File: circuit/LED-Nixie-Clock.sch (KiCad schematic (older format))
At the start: 16 parts, among them SW1 Reset, U1 LM1117-3.3, U2 STM32F103C8Tx

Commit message: Improve schematics, add crystals, USB connector, power regulator, backup battery
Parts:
- added BT1: 3V, Battery:BatteryHolder_Keystone_1058_1x2032, symbol Device:Battery_Cell
- added C10, C11, C12, C13: 20p, Capacitor_SMD:C_0805_2012Metric_Pad1.15x1.40mm_HandSolder, symbol Device:C
- added C5: 100n, Capacitor_SMD:C_0805_2012Metric_Pad1.15x1.40mm_HandSolder, symbol Device:C
- added D1, D2: 1N5817, Diode_SMD:D_0805_2012Metric_Pad1.15x1.40mm_HandSolder, symbol Device:D_Schottky
- added J1: USB Micro, Connector_USB:USB_Micro-B_Molex_47346-0001, symbol Connector:USB_B_Micro
- added R2: 20R, Resistor_SMD:R_0805_2012Metric_Pad1.15x1.40mm_HandSolder, symbol Device:R
- added R3: 4.7k, Resistor_SMD:R_0805_2012Metric_Pad1.15x1.40mm_HandSolder, symbol Device:R
- added Y1: 8MHz, Crystal:Crystal_SMD_HC49-SD, symbol Device:Crystal
- added Y2: 32.768kHz, Crystal:Crystal_SMD_3225-4Pin_3.2x2.5mm, symbol Device:Crystal
- C1, C2, C3, C4: footprint Capacitor_SMD:C_0805_2012Metric -> Capacitor_SMD:C_0805_2012Metric_Pad1.15x1.40mm_HandSolder
- C14: renamed from C9; value 100n -> 1u; footprint Capacitor_SMD:C_0805_2012Metric -> Capacitor_SMD:C_0805_2012Metric_Pad1.15x1.40mm_HandSolder
- C6: renamed from C5; footprint Capacitor_SMD:C_0805_2012Metric -> Capacitor_SMD:C_0805_2012Metric_Pad1.15x1.40mm_HandSolder
- C7: renamed from C6; footprint Capacitor_SMD:C_0805_2012Metric -> Capacitor_SMD:C_0805_2012Metric_Pad1.15x1.40mm_HandSolder
- C8: renamed from C7; footprint Capacitor_SMD:C_0805_2012Metric -> Capacitor_SMD:C_0805_2012Metric_Pad1.15x1.40mm_HandSolder
- C9: renamed from C8; footprint Capacitor_SMD:C_0805_2012Metric -> Capacitor_SMD:C_0805_2012Metric_Pad1.15x1.40mm_HandSolder
- R1: value 10k -> 20R; footprint Resistor_SMD:R_0805_2012Metric -> Resistor_SMD:R_0805_2012Metric_Pad1.15x1.40mm_HandSolder
- R4: renamed from R2; footprint Resistor_SMD:R_0805_2012Metric -> Resistor_SMD:R_0805_2012Metric_Pad1.15x1.40mm_HandSolder
- R5: renamed from R3; footprint Resistor_SMD:R_0805_2012Metric -> Resistor_SMD:R_0805_2012Metric_Pad1.15x1.40mm_HandSolder
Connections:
- net labels added: +BATT, OSC32_IN, OSC32_OUT, OSC_IN, OSC_OUT, USBDM, USBDP, VBUS
- net labels removed: VCC, VDC
- wire segments 54 -> 103
- no-connect marks 37 -> 31
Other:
- moved on the sheet: C1, C14, C2, C3, C4, C6, C7, C8, C9, JP1, R4, R5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

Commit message: Add a test point at DOUT of the last LED
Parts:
- added TP1: DOUT, TestPoint:TestPoint_Pad_1.0x1.0mm, symbol Connector:TestPoint
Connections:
- no-connect marks 31 -> 30
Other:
- moved on the sheet: C6, C7, C8, C9, R5, U2

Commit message: Use MCP1700 linear regulator instead of LM1117
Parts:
- removed C2, C4: 100n, Capacitor_SMD:C_0805_2012Metric_Pad1.15x1.40mm_HandSolder, symbol Device:C
- removed U1: LM1117-3.3, Package_TO_SOT_SMD:SOT-223-3_TabPin2, symbol Regulator_Linear:LM1117-3.3
- added U1: MCP1700-3302E_SOT23, Package_TO_SOT_SMD:SOT-23_Handsoldering, symbol Regulator_Linear:MCP1700-3302E_SOT23
- C2: renamed from C3; value 10u -> 1u
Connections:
- wire segments 103 -> 95
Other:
- moved on the sheet: C2
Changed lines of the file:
@@
 L power:VDD #PWR0110
 U 1 1 5C3A07BC
-P 4800 900
-F 0 "#PWR0110" H 4800 750 50  0001 C CNN
-F 1 "VDD" H 4817 1073 50  0000 C CNN
-F 2 "" H 4800 900 50  0001 C CNN
-F 3 "" H 4800 900 50  0001 C CNN
-	1    4800 900
+P 4100 900
+F 0 "#PWR0110" H 4100 750 50  0001 C CNN
+F 1 "VDD" H 4117 1073 50  0000 C CNN
+F 2 "" H 4100 900 50  0001 C CNN
+F 3 "" H 4100 900 50  0001 C CNN
+	1    4100 900
 	1    0    0    -1
 $EndComp
@@
 	4900 5200 4800 5200
 $Comp
-L Regulator_Linear:LM1117-3.3 U1
-U 1 1 5C415EF9
-P 3900 900
-F 0 "U1" H 3900 1142 50  0000 C CNN
-F 1 "LM1117-3.3" H 3900 1051 50  0000 C CNN
-F 2 "Package_TO_SOT_SMD:SOT-223-3_TabPin2" H 3900 900 50  0001 C CNN
-F 3 "http://www.ti.com/lit/ds/symlink/lm1117.pdf" H 3900 900 50  0001 C CNN
-	1    3900 900
-	1    0    0    -1
-$EndComp
-$Comp
-L Device:C C3
+L Device:C C2
 U 1 1 5C424CF6
-P 4400 1250
-F 0 "C3" H 4515 1296 50  0000 L CNN
-F 1 "10u" H 4515 1205 50  0000 L CNN
-F 2 "Capacitor_SMD:C_0805_2012Metric_Pad1.15x1.40mm_HandSolder" H 4438 1100 50  0001 C CNN
-F 3 "~" H 4400 1250 50  0001 C CNN
-	1    4400 1250
-	1    0    0    -1
-$EndComp
-$Comp
-L Device:C C4
-U 1 1 5C424ED1
-P 4800 1250
-F 0 "C4" H 4915 1296 50  0000 L CNN
-F 1 "100n" H 4915 1205 50  0000 L CNN
-F 2 "Capacitor_SMD:C_0805_2012Metric_Pad1.15x1.40mm_HandSolder" H 4838 1100 50  0001 C CNN
-F 3 "~" H 4800 1250 50  0001 C CNN
-	1    4800 1250
-	1    0    0    -1
-$EndComp
-$Comp
-L Device:C C2
-U 1 1 5C4295B3
-P 3300 1250
-F 0 "C2" H 3415 1296 50  0000 L CNN
-F 1 "100n" H 3415 1205 50  0000 L CNN
-F 2 "Capacitor_SMD:C_0805_2012Metric_Pad1.15x1.40mm_HandSolder" H 3338 1100 50  0001 C CNN
-F 3 "~" H 3300 1250 50  0001 C CNN
-	1    3300 1250
+P 4100 1250
+F 0 "C2" H 4215 1296 50  0000 L CNN
+F 1 "1u" H 4215 1205 50  0000 L CNN
+F 2 "Capacitor_SMD:C_0805_2012Metric_Pad1.15x1.40mm_HandSolder" H 4138 1100 50  0001 C CNN
+F 3 "~" H 4100 1250 50  0001 C CNN
+	1    4100 1250
 	1    0    0    -1
 $EndComp
@@
 	2900 900  2900 1100
 Wire Wire Line
-	4200 900  4400 900
-Wire Wire Line
-	2900 900  3300 900
+	3800 900  4100 900
+Wire Wire Line
+	2900 900  3200 900
 Wire Wire Line
 	2900 1400 2900 1600
 Wire Wire Line
-	2900 1600 3300 1600
-Wire Wire Line
-	3300 1100 3300 900
-Connection ~ 3300 900
-Wire Wire Line
-	3300 900  3600 900
-Wire Wire Line
-	3300 1400 3300 1600
-Connection ~ 3300 1600
-Wire Wire Line
-	3300 1600 3900 1600
-Wire Wire Line
-	4400 1100 4400 900
-Connection ~ 4400 900
-Wire Wire Line
-	4400 900  4800 900
-Wire Wire Line
-	3900 1200 3900 1600
-Connection ~ 3900 1600
-Wire Wire Line
-	3900 1600 4400 1600
-Wire Wire Line
-	4400 1400 4400 1600
-Connection ~ 4400 1600
-Wire Wire Line
-	4400 1600 4800 1600
-Wire Wire Line
-	4800 1400 4800 1600
-Wire Wire Line
-	4800 1100 4800 900
-Connection ~ 4800 900
-Connection ~ 2900 1600
+	4100 1100 4100 900
+Connection ~ 4100 900
+Wire Wire Line
+	3500 1200 3500 1600
+Wire Wire Line
+	3500 1600 4100 1600
+Wire Wire Line
+	4100 1400 4100 1600
 Wire Wire Line
 	2500 900  2900 900
@@
 	0    1    1    0
 $EndComp
+$Comp
+L Regulator_Linear:MCP1700-3302E_SOT23 U1
+U 1 1 5C8BC8BE
+P 3500 900
+F 0 "U1" H 3500 1142 50  0000 C CNN
+F 1 "MCP1700-3302E_SOT23" H 3500 1051 50  0000 C CNN
+F 2 "Package_TO_SOT_SMD:SOT-23_Handsoldering" H 3500 1125 50  0001 C CNN
+F 3 "http://ww1.microchip.com/downloads/en/DeviceDoc/20001826C.pdf" H 3500 900 50  0001 C CNN
+	1    3500 900
+	1    0    0    -1
+$EndComp
+Wire Wire Line
+	2900 1600 3500 1600
+Connection ~ 2900 1600
+Connection ~ 3500 1600
 $EndSCHEMATC

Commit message: Add mounting holes
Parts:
- added H1, H2, H3, H4, H5, H6: MountingHole, MountingHole:MountingHole_3.2mm_M3_ISO7380, symbol Mechanical:MountingHole
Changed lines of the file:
@@
 Connection ~ 2900 1600
 Connection ~ 3500 1600
+$Comp
+L Mechanical:MountingHole H6
+U 1 1 5C8F568C
+P 600 7700
+F 0 "H6" H 700 7746 50  0000 L CNN
+F 1 "MountingHole" H 700 7655 50  0000 L CNN
+F 2 "MountingHole:MountingHole_3.2mm_M3_ISO7380" H 600 7700 50  0001 C CNN
+F 3 "~" H 600 7700 50  0001 C CNN
+	1    600  7700
+	1    0    0    -1
+$EndComp
+$Comp
+L Mechanical:MountingHole H5
+U 1 1 5C8F5A1B
+P 600 7500
+F 0 "H5" H 700 7546 50  0000 L CNN
+F 1 "MountingHole" H 700 7455 50  0000 L CNN
+F 2 "MountingHole:MountingHole_3.2mm_M3_ISO7380" H 600 7500 50  0001 C CNN
+F 3 "~" H 600 7500 50  0001 C CNN
+	1    600  7500
+	1    0    0    -1
+$EndComp
+$Comp
+L Mechanical:MountingHole H4
+U 1 1 5C8F5ADF
+P 600 7300
+F 0 "H4" H 700 7346 50  0000 L CNN
+F 1 "MountingHole" H 700 7255 50  0000 L CNN
+F 2 "MountingHole:MountingHole_3.2mm_M3_ISO7380" H 600 7300 50  0001 C CNN
+F 3 "~" H 600 7300 50  0001 C CNN
+	1    600  7300
+	1    0    0    -1
+$EndComp
+$Comp
+L Mechanical:MountingHole H3
+U 1 1 5C8F5CA1
+P 600 7100
+F 0 "H3" H 700 7146 50  0000 L CNN
+F 1 "MountingHole" H 700 7055 50  0000 L CNN
+F 2 "MountingHole:MountingHole_3.2mm_M3_ISO7380" H 600 7100 50  0001 C CNN
+F 3 "~" H 600 7100 50  0001 C CNN
+	1    600  7100
+	1    0    0    -1
+$EndComp
+$Comp
+L Mechanical:MountingHole H2
+U 1 1 5C8F5DF1
+P 600 6900
+F 0 "H2" H 700 6946 50  0000 L CNN
+F 1 "MountingHole" H 700 6855 50  0000 L CNN
+F 2 "MountingHole:MountingHole_3.2mm_M3_ISO7380" H 600 6900 50  0001 C CNN
+F 3 "~" H 600 6900 50  0001 C CNN
+	1    600  6900
+	1    0    0    -1
+$EndComp
+$Comp
+L Mechanical:MountingHole H1
+U 1 1 5C8F5EE9
+P 600 6700
+F 0 "H1" H 700 6746 50  0000 L CNN
+F 1 "MountingHole" H 700 6655 50  0000 L CNN
+F 2 "MountingHole:MountingHole_3.2mm_M3_ISO7380" H 600 6700 50  0001 C CNN
+F 3 "~" H 600 6700 50  0001 C CNN
+	1    600  6700
+	1    0    0    -1
+$EndComp
 $EndSCHEMATC

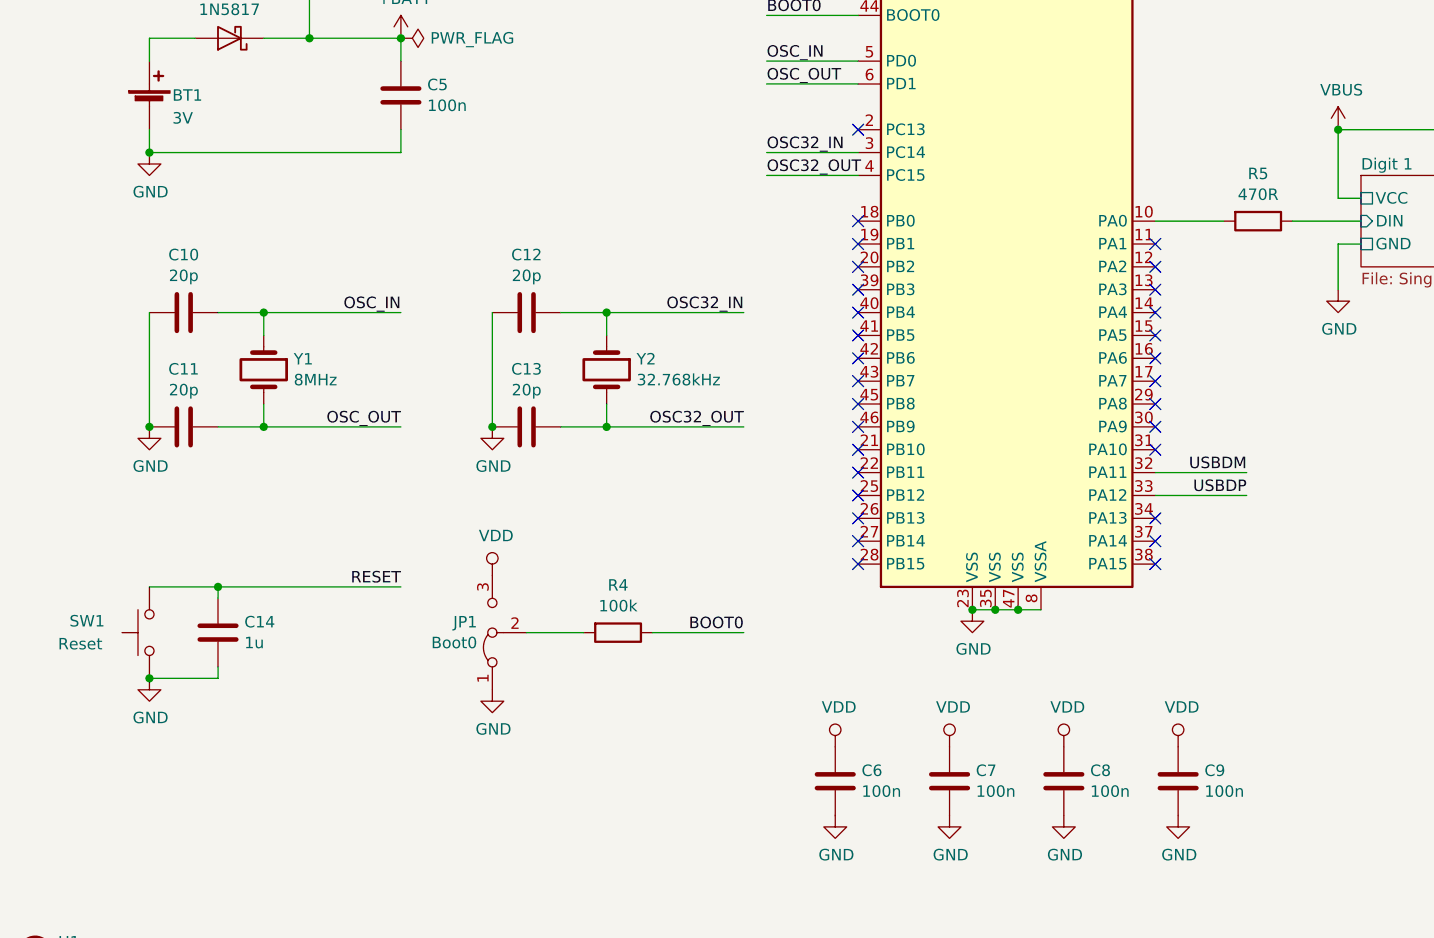
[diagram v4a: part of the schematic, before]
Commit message: Add proper boot jumper and fix some footprints
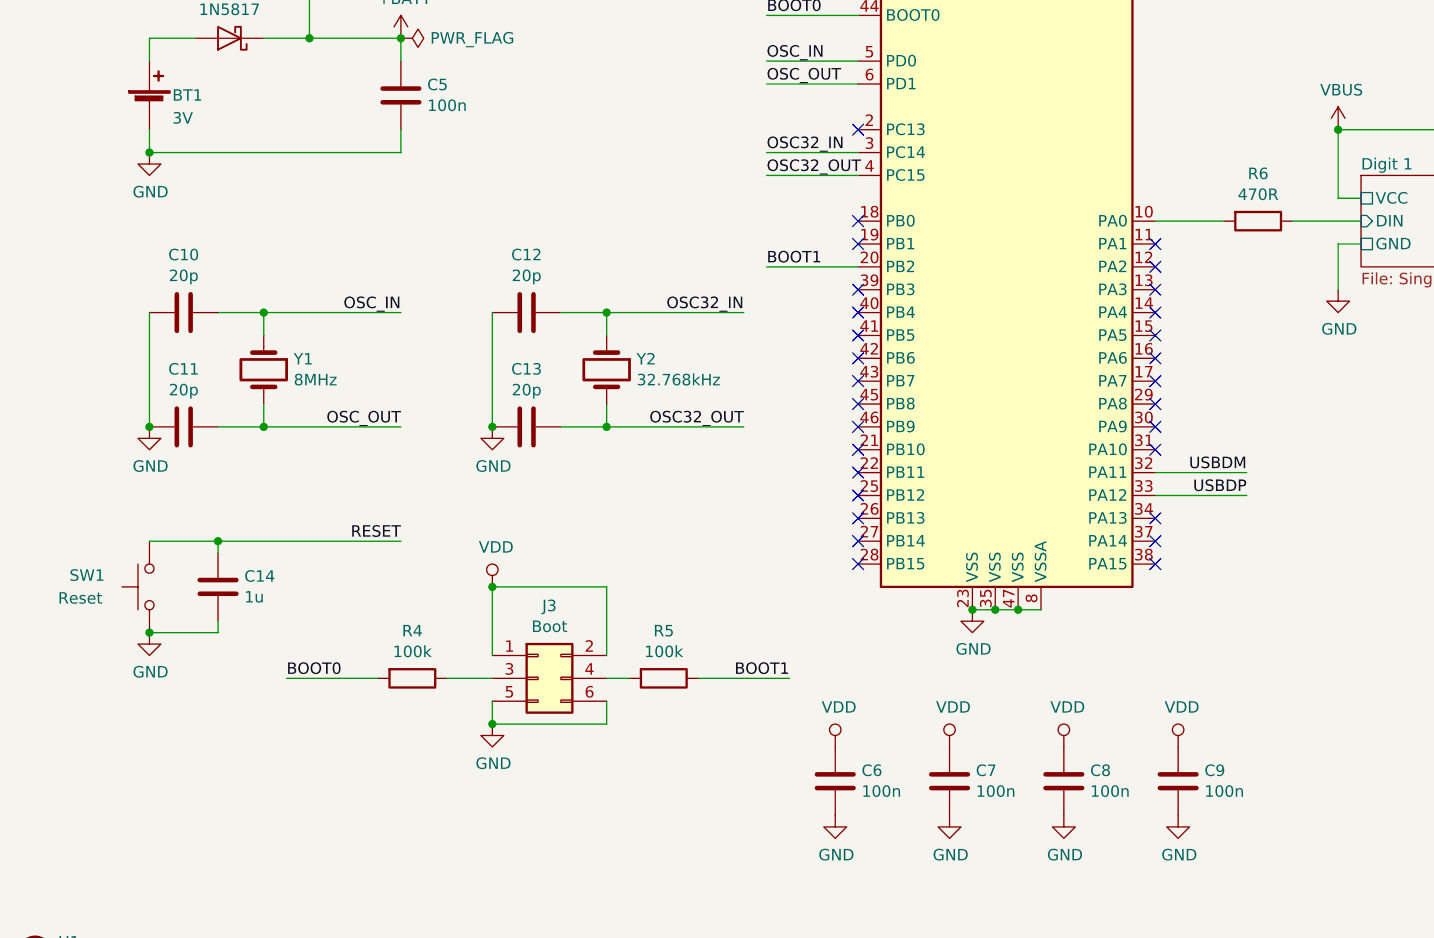
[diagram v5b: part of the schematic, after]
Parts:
- removed JP1: Boot0, Connector_PinHeader_2.54mm:PinHeader_1x03_P2.54mm_Vertical, symbol Jumper:Jumper_3_Bridged12
- added J3: Boot, Connector_PinHeader_2.54mm:PinHeader_2x03_P2.54mm_Vertical, symbol Connector_Generic:Conn_02x03_Odd_Even
- added R5: 100k, Resistor_SMD:R_0805_2012Metric_Pad1.15x1.40mm_HandSolder, symbol Device:R
- J1: footprint Connector_USB:USB_Micro-B_Molex_47346-0001 -> Connector_USB:USB_Micro-B_Wuerth_629105150521
- U2: footprint Package_QFP:LQFP-48-1EP_7x7mm_P0.5mm_EP3.6x3.6mm -> Package_QFP:LQFP-48_7x7mm_P0.5mm
- Y2: footprint Crystal:Crystal_SMD_3225-4Pin_3.2x2.5mm -> Crystal:Crystal_SMD_3215-2Pin_3.2x1.5mm
- renumbered R5 to R6
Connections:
- net BOOT0: now also R4.2; no longer R4.1
- net GND: now also J3.5 (Pin_5), J3.6 (Pin_6)
- net VDD: now also J3.1 (Pin_1), J3.2 (Pin_2)
- net BOOT1: now reaches U2.20 (PB2)
- net BOOT1: now also R5.1
- new net: J3.3 (Pin_3), R4.1
- new net: J3.4 (Pin_4), R5.2
- no-connect marks 30 -> 29
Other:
- moved on the sheet: C14, R4, SW1
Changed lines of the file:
@@
 F 0 "U2" H 5350 5350 50  0000 C CNN
 F 1 "STM32F103C8Tx" H 5600 5250 50  0000 C CNN
-F 2 "Package_QFP:LQFP-48-1EP_7x7mm_P0.5mm_EP3.6x3.6mm" H 4300 2300 50  0001 R CNN
+F 2 "Package_QFP:LQFP-48_7x7mm_P0.5mm" H 4300 2300 50  0001 R CNN
 F 3 "http://www.st.com/st-web-ui/static/active/en/resource/technical/document/datasheet/CD00161566.pdf" H 4900 3700 50  0001 C CNN
 	1    4900 3700
@@
 NoConn ~ 4200 3500
 NoConn ~ 4200 3600
-NoConn ~ 4200 3700
 NoConn ~ 4200 3800
 NoConn ~ 4200 3900
@@
 NoConn ~ 5500 3600
 $Comp
-L Device:R R5
+L Device:R R6
 U 1 1 5C3A0157
 P 5950 3500
-F 0 "R5" V 5743 3500 50  0000 C CNN
+F 0 "R6" V 5743 3500 50  0000 C CNN
 F 1 "470R" V 5834 3500 50  0000 C CNN
 F 2 "Resistor_SMD:R_0805_2012Metric_Pad1.15x1.40mm_HandSolder" V 5880 3500 50  0001 C CNN
@@
 	6300 3600 6300 3800
 $Comp
-L Jumper:Jumper_3_Bridged12 JP1
-U 1 1 5C3F92DA
-P 2600 5300
-F 0 "JP1" V 2646 5366 50  0000 L CNN
-F 1 "Boot0" V 2555 5366 50  0000 L CNN
-F 2 "Connector_PinHeader_2.54mm:PinHeader_1x03_P2.54mm_Vertical" H 2600 5300 50  0001 C CNN
-F 3 "~" H 2600 5300 50  0001 C CNN
-	1    2600 5300
-	0    -1   -1   0
-$EndComp
-$Comp
 L power:VDD #PWR0157
 U 1 1 5C3F9616
-P 2600 5050
-F 0 "#PWR0157" H 2600 4900 50  0001 C CNN
-F 1 "VDD" H 2617 5223 50  0000 C CNN
-F 2 "" H 2600 5050 50  0001 C CNN
-F 3 "" H 2600 5050 50  0001 C CNN
-	1    2600 5050
+P 2600 5100
+F 0 "#PWR0157" H 2600 4950 50  0001 C CNN
+F 1 "VDD" H 2617 5273 50  0000 C CNN
+F 2 "" H 2600 5100 50  0001 C CNN
+F 3 "" H 2600 5100 50  0001 C CNN
+	1    2600 5100
 	1    0    0    -1
 $EndComp
@@
 L power:GND #PWR0158
 U 1 1 5C3F968A
-P 2600 5550
-F 0 "#PWR0158" H 2600 5300 50  0001 C CNN
-F 1 "GND" H 2605 5377 50  0000 C CNN
-F 2 "" H 2600 5550 50  0001 C CNN
-F 3 "" H 2600 5550 50  0001 C CNN
-	1    2600 5550
+P 2600 5700
+F 0 "#PWR0158" H 2600 5450 50  0001 C CNN
+F 1 "GND" H 2605 5527 50  0000 C CNN
+F 2 "" H 2600 5700 50  0001 C CNN
+F 3 "" H 2600 5700 50  0001 C CNN
+	1    2600 5700
 	1    0    0    -1
 $EndComp
@@
 L Device:R R4
 U 1 1 5C3F97D4
-P 3150 5300
-F 0 "R4" V 2943 5300 50  0000 C CNN
-F 1 "100k" V 3034 5300 50  0000 C CNN
-F 2 "Resistor_SMD:R_0805_2012Metric_Pad1.15x1.40mm_HandSolder" V 3080 5300 50  0001 C CNN
-F 3 "~" H 3150 5300 50  0001 C CNN
-	1    3150 5300
-	0    1    1    0
-$EndComp
-Wire Wire Line
-	3000 5300 2750 5300
+P 2250 5500
+F 0 "R4" V 2043 5500 50  0000 C CNN
+F 1 "100k" V 2134 5500 50  0000 C CNN
+F 2 "Resistor_SMD:R_0805_2012Metric_Pad1.15x1.40mm_HandSolder" V 2180 5500 50  0001 C CNN
+F 3 "~" H 2250 5500 50  0001 C CNN
+	1    2250 5500
+	0    1    1    0
+$EndComp
 $Comp
 L power:GND #PWR0160
@@
 	1    0    0    -1
 $EndComp
-Text Label 3700 5300 2    50   ~ 0
+Text Label 1700 5500 0    50   ~ 0
 BOOT0
 Wire Wire Line
-	3300 5300 3700 5300
+	3500 5500 3900 5500
 Wire Wire Line
 	3800 2600 4200 2600
@@
 L Switch:SW_Push SW1
 U 1 1 5C405137
-P 1100 5300
-F 0 "SW1" V 1150 5650 50  0000 R CNN
-F 1 "Reset" V 1050 5700 50  0000 R CNN
-F 2 "Button_Switch_SMD:SW_SPST_CK_RS282G05A3" H 1100 5500 50  0001 C CNN
-F 3 "" H 1100 5500 50  0001 C CNN
-	1    1100 5300
+P 1100 5100
+F 0 "SW1" V 1150 5450 50  0000 R CNN
+F 1 "Reset" V 1050 5500 50  0000 R CNN
+F 2 "Button_Switch_SMD:SW_SPST_CK_RS282G05A3" H 1100 5300 50  0001 C CNN
+F 3 "" H 1100 5300 50  0001 C CNN
+	1    1100 5100
 	0    -1   -1   0
 $EndComp
@@
 L power:GND #PWR0115
 U 1 1 5C4057E8
-P 1100 5500
-F 0 "#PWR0115" H 1100 5250 50  0001 C CNN
-F 1 "GND" H 1105 5327 50  0000 C CNN
-F 2 "" H 1100 5500 50  0001 C CNN
-F 3 "" H 1100 5500 50  0001 C CNN
-	1    1100 5500
+P 1100 5300
+F 0 "#PWR0115" H 1100 5050 50  0001 C CNN
+F 1 "GND" H 1105 5127 50  0000 C CNN
+F 2 "" H 1100 5300 50  0001 C CNN
+F 3 "" H 1100 5300 50  0001 C CNN
+	1    1100 5300
 	1    0    0    -1
 $EndComp
@@
 L Device:C C14
 U 1 1 5C405E01
-P 1400 5300
-F 0 "C14" H 1515 5346 50  0000 L CNN
-F 1 "1u" H 1515 5255 50  0000 L CNN
-F 2 "Capacitor_SMD:C_0805_2012Metric_Pad1.15x1.40mm_HandSolder" H 1438 5150 50  0001 C CNN
-F 3 "~" H 1400 5300 50  0001 C CNN
-	1    1400 5300
-	1    0    0    -1
-$EndComp
-Connection ~ 1100 5500
-Wire Wire Line
-	1100 5100 1400 5100
-Wire Wire Line
-	1400 5100 1400 5150
-Wire Wire Line
-	1400 5450 1400 5500
-Wire Wire Line
-	1400 5500 1100 5500
+P 1400 5100
+F 0 "C14" H 1515 5146 50  0000 L CNN
+F 1 "1u" H 1515 5055 50  0000 L CNN
+F 2 "Capacitor_SMD:C_0805_2012Metric_Pad1.15x1.40mm_HandSolder" H 1438 4950 50  0001 C CNN
+F 3 "~" H 1400 5100 50  0001 C CNN
+	1    1400 5100
+	1    0    0    -1
+$EndComp
+Connection ~ 1100 5300
+Wire Wire Line
+	1100 4900 1400 4900
+Wire Wire Line
+	1400 4900 1400 4950
+Wire Wire Line
+	1400 5250 1400 5300
+Wire Wire Line
+	1400 5300 1100 5300
 Wire Wire Line
 	6300 3100 7400 3100
@@
 	7400 3100 8500 3100
 Wire Wire Line
-	1400 5100 2200 5100
-Connection ~ 1400 5100
-Text Label 2200 5100 2    50   ~ 0
+	1400 4900 2200 4900
+Connection ~ 1400 4900
+Text Label 2200 4900 2    50   ~ 0
 RESET
 Connection ~ 4800 2200
@@
 F 0 "Y2" V 3054 4281 50  0000 L CNN
 F 1 "32.768kHz" V 3145 4281 50  0000 L CNN
-F 2 "Crystal:Crystal_SMD_3225-4Pin_3.2x2.5mm" H 3100 4150 50  0001 C CNN
+F 2 "Crystal:Crystal_SMD_3215-2Pin_3.2x1.5mm" H 3100 4150 50  0001 C CNN
 F 3 "~" H 3100 4150 50  0001 C CNN
 	1    3100 4150
@@
 F 0 "J1" H 1055 1567 50  0000 C CNN
 F 1 "USB Micro" H 1055 1476 50  0000 C CNN
-F 2 "Connector_USB:USB_Micro-B_Molex_47346-0001" H 1150 1050 50  0001 C CNN
+F 2 "Connector_USB:USB_Micro-B_Wuerth_629105150521" H 1150 1050 50  0001 C CNN
 F 3 "~" H 1150 1050 50  0001 C CNN
 	1    1000 1100
@@
 	1    0    0    -1
 $EndComp
+Wire Wire Line
+	4200 3700 3800 3700
+Text Label 3800 3700 0    50   ~ 0
+BOOT1
+$Comp
+L Connector_Generic:Conn_02x03_Odd_Even J3
+U 1 1 5C904E0F
+P 2800 5500
+F 0 "J3" H 2850 5817 50  0000 C CNN
+F 1 "Boot" H 2850 5726 50  0000 C CNN
+F 2 "Connector_PinHeader_2.54mm:PinHeader_2x03_P2.54mm_Vertical" H 2800 5500 50  0001 C CNN
+F 3 "~" H 2800 5500 50  0001 C CNN
+	1    2800 5500
+	1    0    0    -1
+$EndComp
+Wire Wire Line
+	3200 5500 3100 5500
+$Comp
+L Device:R R5
+U 1 1 5C918657
+P 3350 5500
+F 0 "R5" V 3143 5500 50  0000 C CNN
+F 1 "100k" V 3234 5500 50  0000 C CNN
+F 2 "Resistor_SMD:R_0805_2012Metric_Pad1.15x1.40mm_HandSolder" V 3280 5500 50  0001 C CNN
+F 3 "~" H 3350 5500 50  0001 C CNN
+	1    3350 5500
+	0    1    1    0
+$EndComp
+Wire Wire Line
+	2600 5500 2400 5500
+Wire Wire Line
+	2600 5400 2600 5100
+Wire Wire Line
+	2600 5100 3100 5100
+Wire Wire Line
+	3100 5100 3100 5400
+Wire Wire Line
+	2600 5600 2600 5700
+Wire Wire Line
+	2600 5700 3100 5700
+Wire Wire Line
+	3100 5700 3100 5600
+Wire Wire Line
+	2100 5500 1700 5500
+Text Label 3900 5500 2    50   ~ 0
+BOOT1
+Connection ~ 2600 5100
+Connection ~ 2600 5700
 $EndSCHEMATC
